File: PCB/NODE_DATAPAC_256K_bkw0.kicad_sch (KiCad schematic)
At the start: 28 parts, among them J1 Conn_02x20_Odd_Even, U1 74161, U10 62256, U2 74161, U3 74161, U4 74138, U5 74138, U6 74374, U7 62256, U8 62256, U9 62256

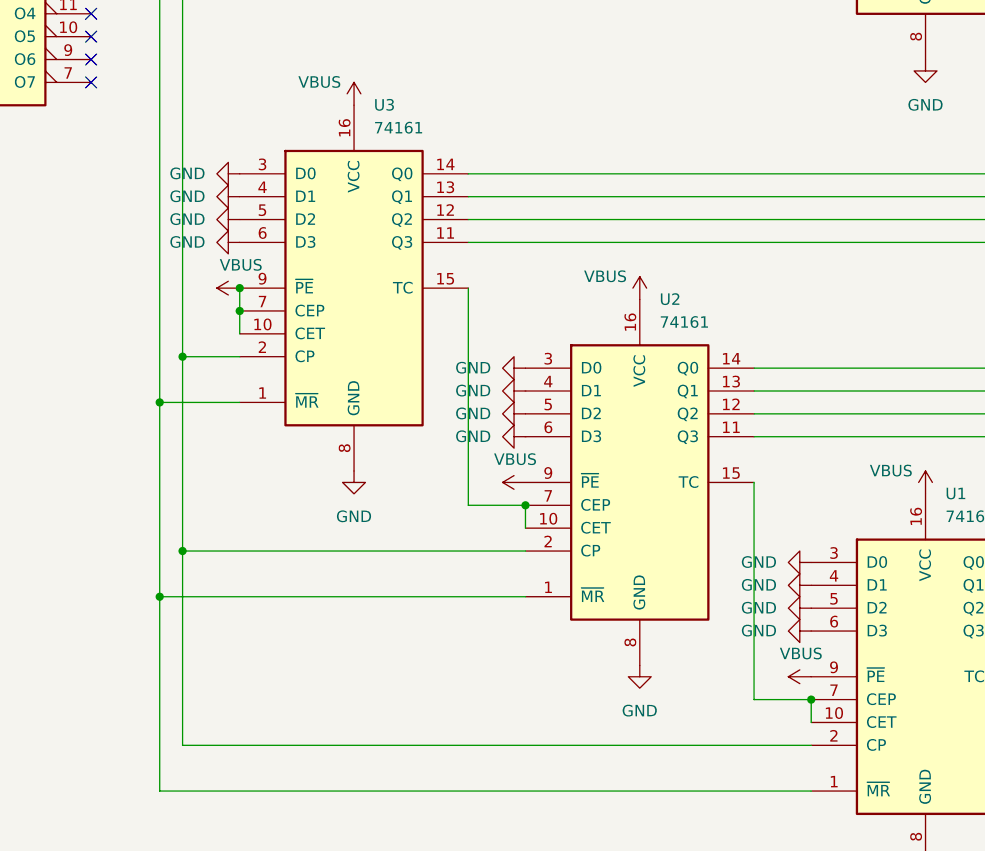
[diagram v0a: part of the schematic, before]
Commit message: remove unused 3d models
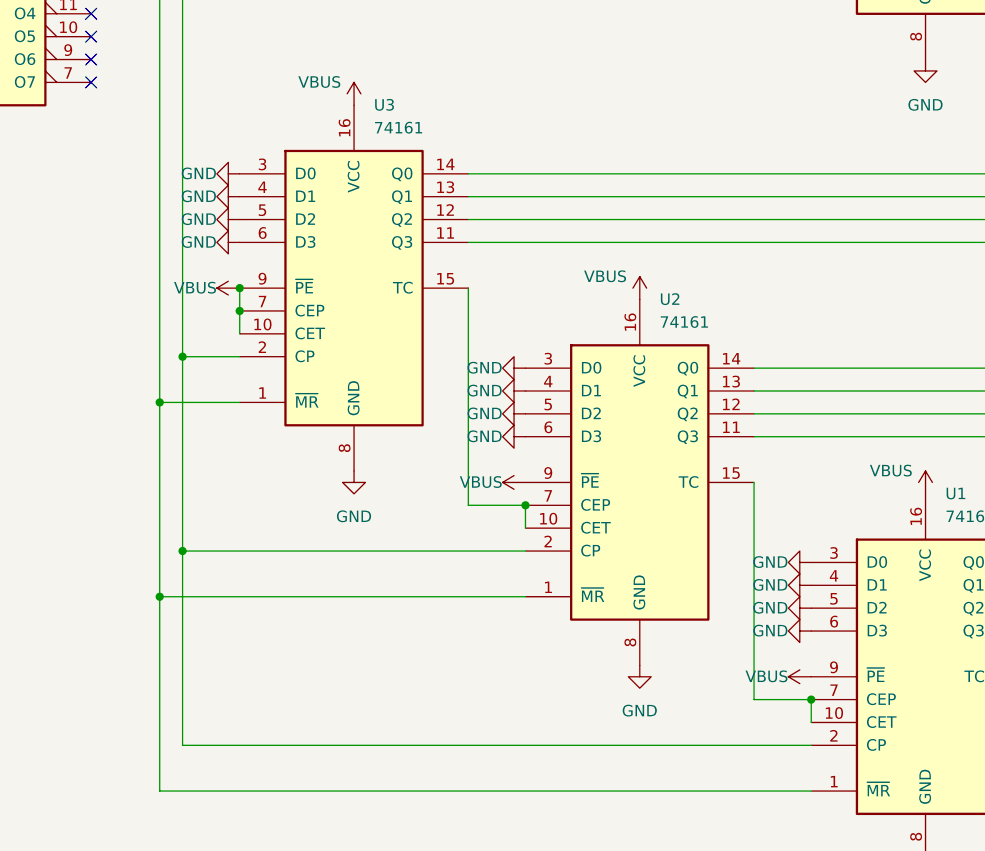
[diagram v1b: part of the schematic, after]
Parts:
- C1, C2, C3, C4, C5: footprint 000_LOCAL:C_Disc_D3.0mm_W1.6mm_P2.50mm -> 000_LOCAL:C_cer_tht_p2.5

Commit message: readme, software, remove nimh from new board
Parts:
- removed BT1: FL3/V80H, 000_LOCAL:CONN2_1776275-2, symbol 000_LOCAL:Screw_Terminal_01x02
- removed R1: 200, 000_LOCAL:R_Axial_DIN0207_L6.3mm_D2.5mm_P10.16mm_Horizontal, symbol 000_LOCAL:R
- U10, U7, U8, U9: symbol 000_LOCAL:62256-DIP -> 000_LOCAL:62256
- renumbered BT2 to BT1
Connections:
- net BATT+: now also BT1.1 (+), D3.2 (A)
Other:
- note removed: "Only one of either BT1 or BT2 is required."
- note removed: "non-rechargeable"
- note removed: "rechargeable 3.6V NiCD or NiMH"
- moved on the sheet: BT1, D1, D3

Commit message: truth table
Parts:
- added C6, C7: 0.1u, 000_LOCAL:C_cer_tht_p2.5, symbol 000_LOCAL:C
- renumbered D3 to D2, D2 to D3, U3 to U1, U1 to U3
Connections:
- net A10: now also U10.8 (A2), U2.13 (Q1), U7.3 (A7), U8.8 (A2), U9.3 (A7); no longer J1.15 (Pin_15)
- net A11: now also U10.7 (A3), U2.12 (Q2), U7.4 (A6), U8.7 (A3), U9.4 (A6); no longer J1.16 (Pin_16)
- net A12: now also U10.6 (A4), U2.11 (Q3), U7.5 (A5), U8.6 (A4), U9.5 (A5); no longer J1.17 (Pin_17)
- net A13: now also U10.26 (A13), U3.14 (Q0), U7.21 (A10), U8.26 (A13), U9.21 (A10); no longer J1.18 (Pin_18)
- net A14: now also U10.10 (A0), U3.13 (Q1), U7.1 (A14), U8.10 (A0), U9.1 (A14); no longer J1.19 (Pin_19)
- net A15: now also U5.1 (A0), U6.5 (O1); no longer J1.20 (Pin_20)
- net A8: now also U1.11 (Q3), U10.21 (A10), U7.26 (A13), U8.21 (A10), U9.26 (A13); no longer J1.13 (Pin_13), U4.1 (A0)
- net A9: now also U10.9 (A1), U2.14 (Q0), U7.2 (A12), U8.9 (A1), U9.2 (A12); no longer J1.14 (Pin_14), U4.2 (A1)
- net GND: now also C6.2, C7.2
- net VBUS: now also C6.1, C7.1
- net A1: now reaches U10.1 (A14), U6.9 (O3), U7.10 (A0), U8.1 (A14), U9.10 (A0)
- net A2: now reaches U10.2 (A12), U6.12 (O4), U7.9 (A1), U8.2 (A12), U9.9 (A1)
- net A7: now reaches U1.12 (Q2), U10.23 (A11), U7.25 (A8), U8.23 (A11), U9.25 (A8)
- net A6: now reaches U1.13 (Q1), U10.24 (A9), U7.24 (A9), U8.24 (A9), U9.24 (A9)
- net A5: now reaches U1.14 (Q0), U10.25 (A8), U7.23 (A11), U8.25 (A8), U9.23 (A11)
- net A0: now reaches U10.3 (A7), U6.6 (O2), U7.8 (A2), U8.3 (A7), U9.8 (A2)
- net A3: now reaches U10.4 (A6), U6.15 (O5), U7.7 (A3), U8.4 (A6), U9.7 (A3)
- net A4: now reaches U10.5 (A5), U6.16 (O6), U7.6 (A4), U8.5 (A5), U9.6 (A4)
- net A17: now reaches U5.3 (A2), U6.19 (O7)
- net A16: now reaches U5.2 (A1), U6.2 (O0)
- net TC1: now reaches U2.15 (TC), U3.10 (CET), U3.7 (CEP)
- net TC0: now reaches U1.15 (TC), U2.10 (CET), U2.7 (CEP)
- net CLK: no longer names the net of J1.29 (Pin_29)
- net INTA: no longer names the net of J1.34 (Pin_34)
- net INTR: no longer names the net of J1.33 (Pin_33)
- net IO/~{M}: no longer names the net of J1.25 (Pin_25)
- net S0: no longer names the net of J1.26 (Pin_26)
- net S1: no longer names the net of J1.28 (Pin_28)
- net _RAM_RST renamed SLEEP
- net ~{ALE}: no longer names the net of J1.27 (Pin_27)
- net ~{RESET}: no longer names the net of J1.32 (Pin_32)
- new net BUS_A8: J1.13 (Pin_13), U4.1 (A0)
- new net BUS_A9: J1.14 (Pin_14), U4.2 (A1)
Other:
- note added: "3 address lines converted into 8 chip selects"
- note added: "A10"
- note added: "A11"
- note added: "A12"
- note added: "A13"
- note added: "A14"
- note added: "A15"
- note added: "CLK"
- note added: "ENP"
- note added: "ENT"
- note added: "INTA"
- note added: "INTR"
- note added: "IO/~{M}"
- note added: "ON"
- note added: "RCO"
- note added: "S0"
- note added: "S1"
- note added: "advance address once per read?"
- note added: "disable sram during address change?"
- note added: "prevent host battery drain via RAM_RST through R3 to VMEM?"
- note added: "update bus when counter reset?"
- note added: "| U1-U3 | U5 | U6 | | | A8 A9 | ~{MR} CP | ~{CS} | Cp 0 0 | * | | * 1 0 | * * | | 0 1 | * | | * 1 1 | | * | * *=active high or low U1-U3 address advance counter U5 en/disable all sram U6 bus buffer clk"
- note added: "~{ALE}"
- note added: "~{CLR}"
- note added: "~{LOAD}"
- note added: "~{RESET}"
- moved on the sheet: BT1, D1, D2

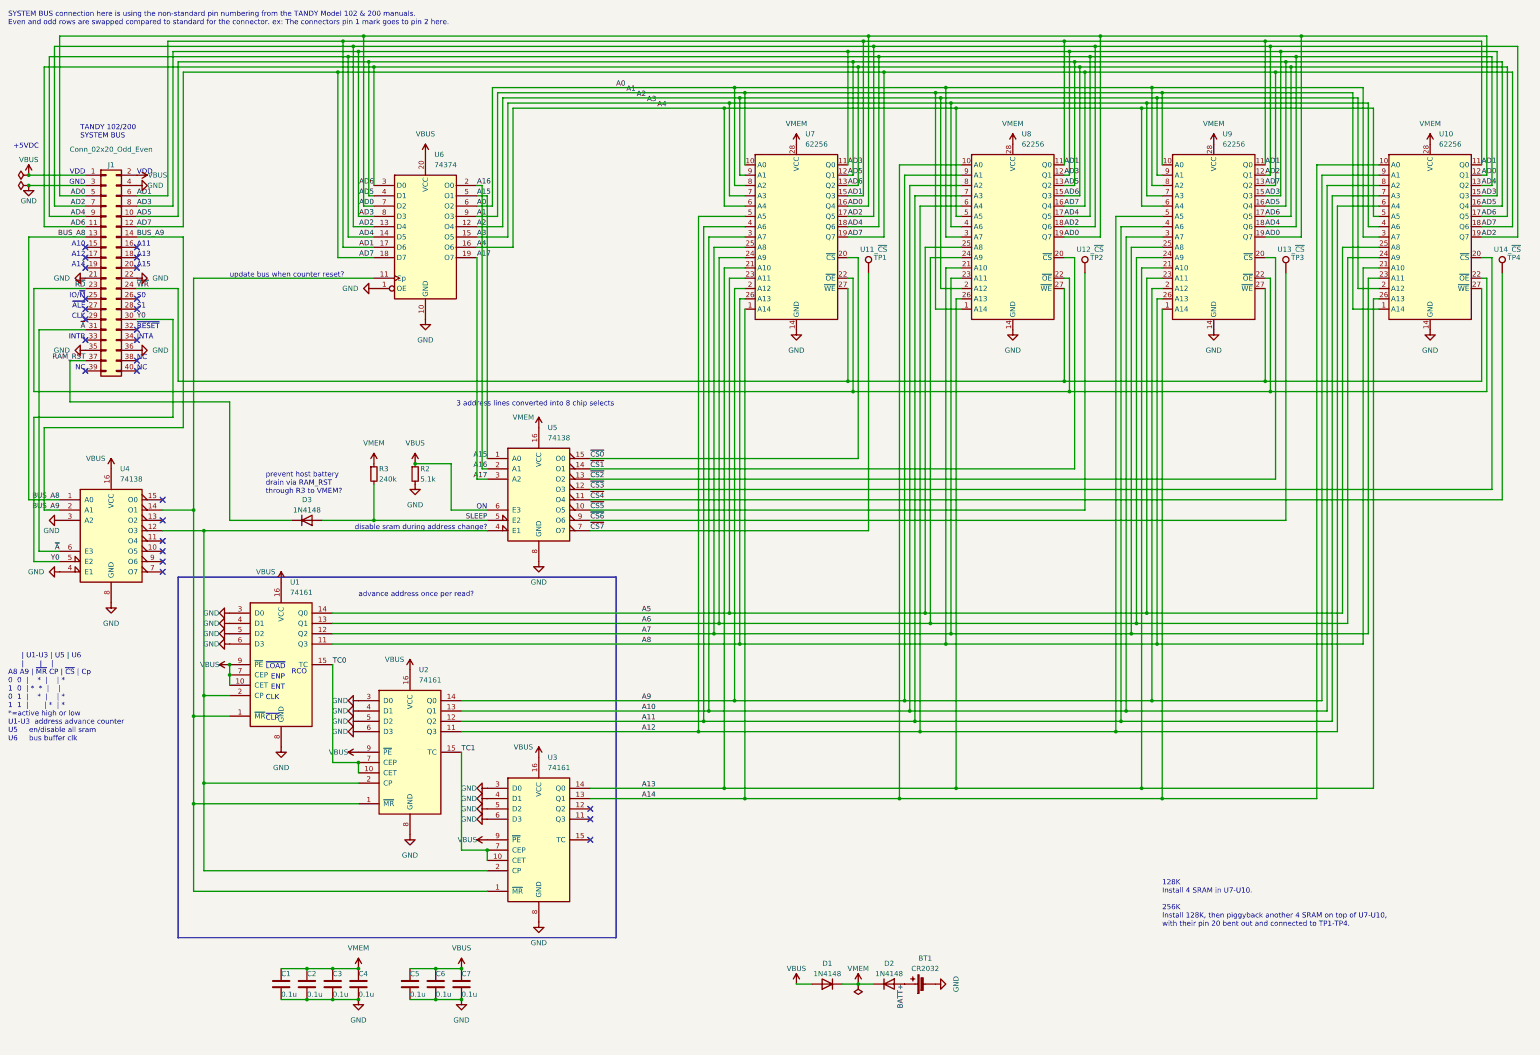
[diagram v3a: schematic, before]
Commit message: start decoding circuit theory of operation, organize files
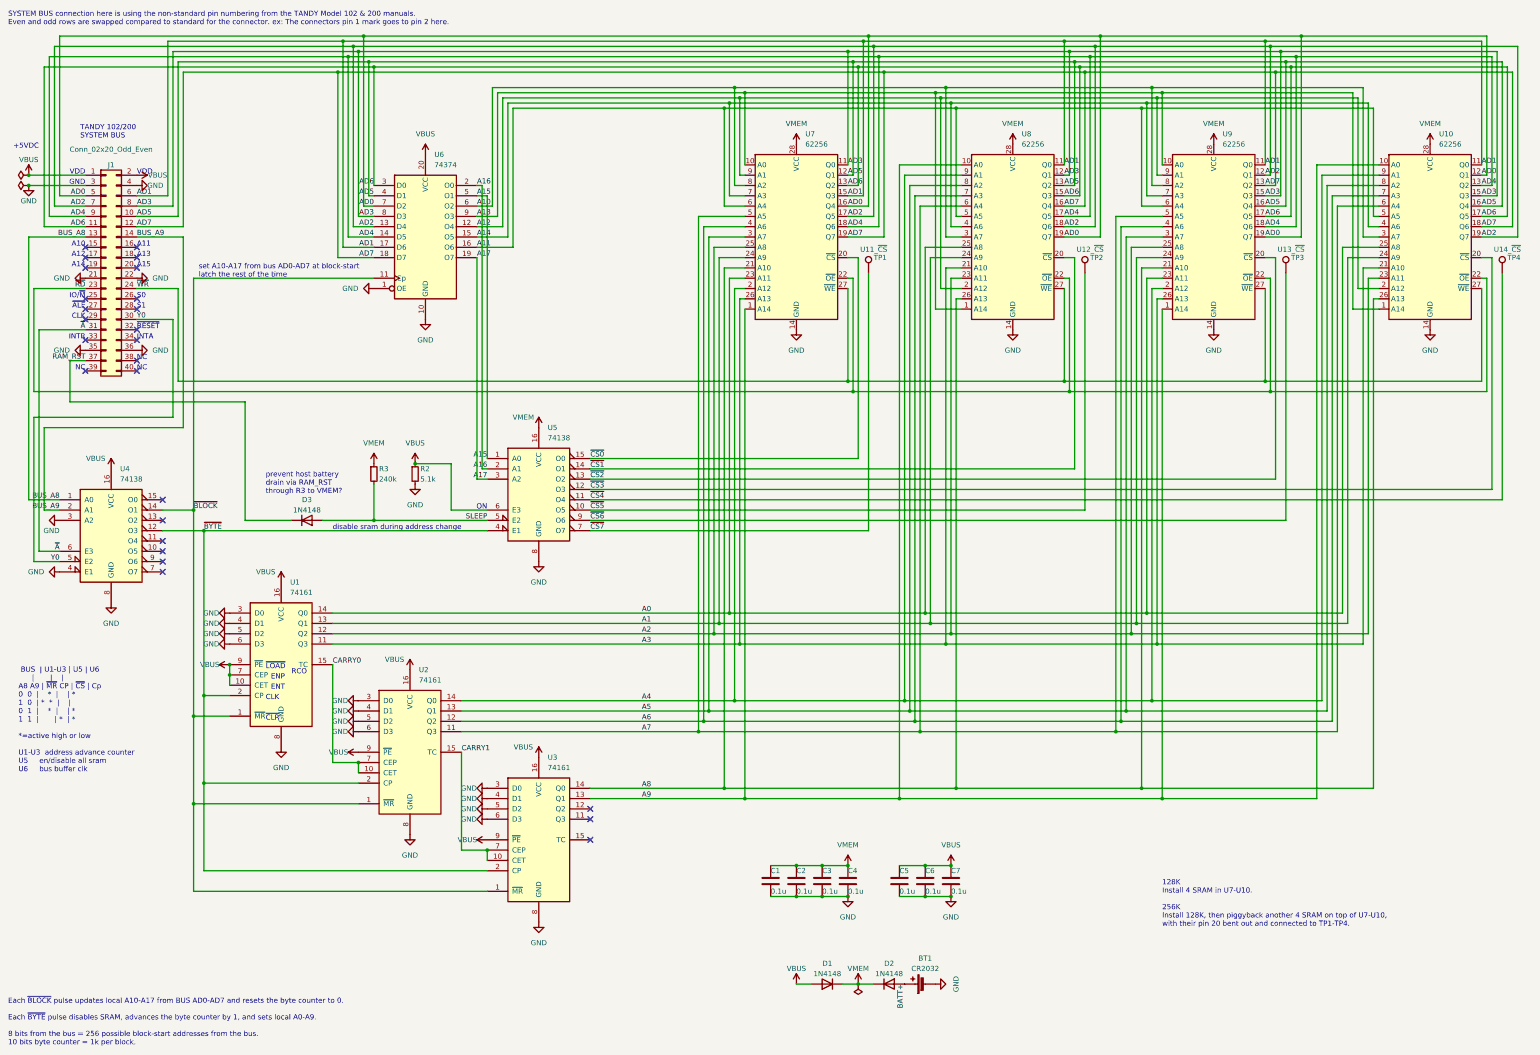
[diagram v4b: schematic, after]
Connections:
- net A0: now also U1.14 (Q0), U10.25 (A8), U7.23 (A11), U8.25 (A8), U9.23 (A11); no longer U10.3 (A7), U6.6 (O2), U7.8 (A2), U8.3 (A7), U9.8 (A2)
- net A1: now also U1.13 (Q1), U10.24 (A9), U7.24 (A9), U8.24 (A9), U9.24 (A9); no longer U10.1 (A14), U6.9 (O3), U7.10 (A0), U8.1 (A14), U9.10 (A0)
- net A10: now also U10.3 (A7), U6.6 (O2), U7.8 (A2), U8.3 (A7), U9.8 (A2); no longer U10.8 (A2), U2.13 (Q1), U7.3 (A7), U8.8 (A2), U9.3 (A7)
- net A11: now also U10.5 (A5), U6.16 (O6), U7.6 (A4), U8.5 (A5), U9.6 (A4); no longer U10.7 (A3), U2.12 (Q2), U7.4 (A6), U8.7 (A3), U9.4 (A6)
- net A12: now also U10.2 (A12), U6.12 (O4), U7.9 (A1), U8.2 (A12), U9.9 (A1); no longer U10.6 (A4), U2.11 (Q3), U7.5 (A5), U8.6 (A4), U9.5 (A5)
- net A13: now also U10.1 (A14), U6.9 (O3), U7.10 (A0), U8.1 (A14), U9.10 (A0); no longer U10.26 (A13), U3.14 (Q0), U7.21 (A10), U8.26 (A13), U9.21 (A10)
- net A14: now also U10.4 (A6), U6.15 (O5), U7.7 (A3), U8.4 (A6), U9.7 (A3); no longer U10.10 (A0), U3.13 (Q1), U7.1 (A14), U8.10 (A0), U9.1 (A14)
- net A2: now also U1.12 (Q2), U10.23 (A11), U7.25 (A8), U8.23 (A11), U9.25 (A8); no longer U10.2 (A12), U6.12 (O4), U7.9 (A1), U8.2 (A12), U9.9 (A1)
- net A3: now also U1.11 (Q3), U10.21 (A10), U7.26 (A13), U8.21 (A10), U9.26 (A13); no longer U10.4 (A6), U6.15 (O5), U7.7 (A3), U8.4 (A6), U9.7 (A3)
- net A4: now also U10.9 (A1), U2.14 (Q0), U7.2 (A12), U8.9 (A1), U9.2 (A12); no longer U10.5 (A5), U6.16 (O6), U7.6 (A4), U8.5 (A5), U9.6 (A4)
- net A5: now also U10.8 (A2), U2.13 (Q1), U7.3 (A7), U8.8 (A2), U9.3 (A7); no longer U1.14 (Q0), U10.25 (A8), U7.23 (A11), U8.25 (A8), U9.23 (A11)
- net A6: now also U10.7 (A3), U2.12 (Q2), U7.4 (A6), U8.7 (A3), U9.4 (A6); no longer U1.13 (Q1), U10.24 (A9), U7.24 (A9), U8.24 (A9), U9.24 (A9)
- net A7: now also U10.6 (A4), U2.11 (Q3), U7.5 (A5), U8.6 (A4), U9.5 (A5); no longer U1.12 (Q2), U10.23 (A11), U7.25 (A8), U8.23 (A11), U9.25 (A8)
- net A8: now also U10.26 (A13), U3.14 (Q0), U7.21 (A10), U8.26 (A13), U9.21 (A10); no longer U1.11 (Q3), U10.21 (A10), U7.26 (A13), U8.21 (A10), U9.26 (A13)
- net A9: now also U10.10 (A0), U3.13 (Q1), U7.1 (A14), U8.10 (A0), U9.1 (A14); no longer U10.9 (A1), U2.14 (Q0), U7.2 (A12), U8.9 (A1), U9.2 (A12)
- net ~{BLOCK}: now reaches U1.1 (~{MR}), U2.1 (~{MR}), U3.1 (~{MR}), U4.14 (O1), U6.11 (Cp)
- net ~{BYTE}: now reaches U1.2 (CP), U2.2 (CP), U3.2 (CP), U4.12 (O3), U5.4 (E1)
- net TC0 renamed CARRY0
- net TC1 renamed CARRY1
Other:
- note added: "BUS | U1-U3 | U5 | U6 | | | A8 A9 | ~{MR} CP | ~{CS} | Cp 0 0 | * | | * 1 0 | * * | | 0 1 | * | | * 1 1 | | * | * *=active high or low U1-U3 address advance counter U5 en/disable all sram U6 bus buffer clk"
- note added: "Each ~{BLOCK} pulse updates local A10-A17 from BUS AD0-AD7 and resets the byte counter to 0. Each ~{BYTE} pulse disables SRAM, advances the byte counter by 1, and sets local A0-A9. 8 bits from the bus = 256 possible block-start addresses from the bus. 10 bits byte counter = 1k per block."
- note added: "disable sram during address change"
- note added: "set A10-A17 from bus AD0-AD7 at block-start latch the rest of the time"
- note removed: "3 address lines converted into 8 chip selects"
- note removed: "advance address once per read?"
- note removed: "disable sram during address change?"
- note removed: "update bus when counter reset?"
- note removed: "| U1-U3 | U5 | U6 | | | A8 A9 | ~{MR} CP | ~{CS} | Cp 0 0 | * | | * 1 0 | * * | | 0 1 | * | | * 1 1 | | * | * *=active high or low U1-U3 address advance counter U5 en/disable all sram U6 bus buffer clk"
- moved on the sheet: C1, C2, C3, C4, C5, C6, C7
